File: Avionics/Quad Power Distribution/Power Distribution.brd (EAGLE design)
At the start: 50 x 50 mm, 56 parts, among them U1 LMP8645, U10 SERVOPLUGTHROUGHHOLE_0.1PITCH, U2 LMP8645, U3 LMP8645, U4 LMP8645, U5 LMP8645, U6 ADP2302, U7 SERVOPLUGTHROUGHHOLE_0.1PITCH, U8 SERVOPLUGTHROUGHHOLE_0.1PITCH, U9 SERVOPLUGTHROUGHHOLE_0.1PITCH

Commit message: Refactored power distrib board libraries into single library
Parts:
- BATT+, GND: device Shared Libraries:10AWG_SOLDERPAD -> PowerDistributionv1:10AWG_SOLDERPAD
- C1, C2, C3, C4: device SparkFun-Capacitors:0603-CAP -> PowerDistributionv1:0603-CAP
- D1: device diode:SMB -> PowerDistributionv1:SMB
- JP1: device Shared Libraries:DF13_6POS -> PowerDistributionv1:DF13_6POS
- JP2: device Shared Libraries:DF13_5POS -> PowerDistributionv1:DF13_5POS
- L1: device SparkFun-Passives:0603 -> PowerDistributionv1:0603
- R1, R2, R3, R4, R5, R6, R7, R8: device Shared Libraries:R2512 -> PowerDistributionv1:R2512
- R10, R11, R12, R13, R14, R15, R16, R17, R18, R19, R20, R21, R22, R23, R9: device Shared Libraries:0603-RES -> PowerDistributionv1:0603-RES
- U1, U2, U3, U4, U5: device Shared Libraries:SOT23-6 -> PowerDistributionv1:SOT23-6
- U10, U7, U8, U9: device Shared Libraries:0.1-PITCH-3CONN -> PowerDistributionv1:0.1-PITCH-3CONN
- U6: device Shared Libraries:SOIC8 -> PowerDistributionv1:SOIC8
- V1+, V1-, V2+, V2-, V3+, V3-, V4+, V4-: device Shared Libraries:5MMPLUG -> PowerDistributionv1:5MMPLUG

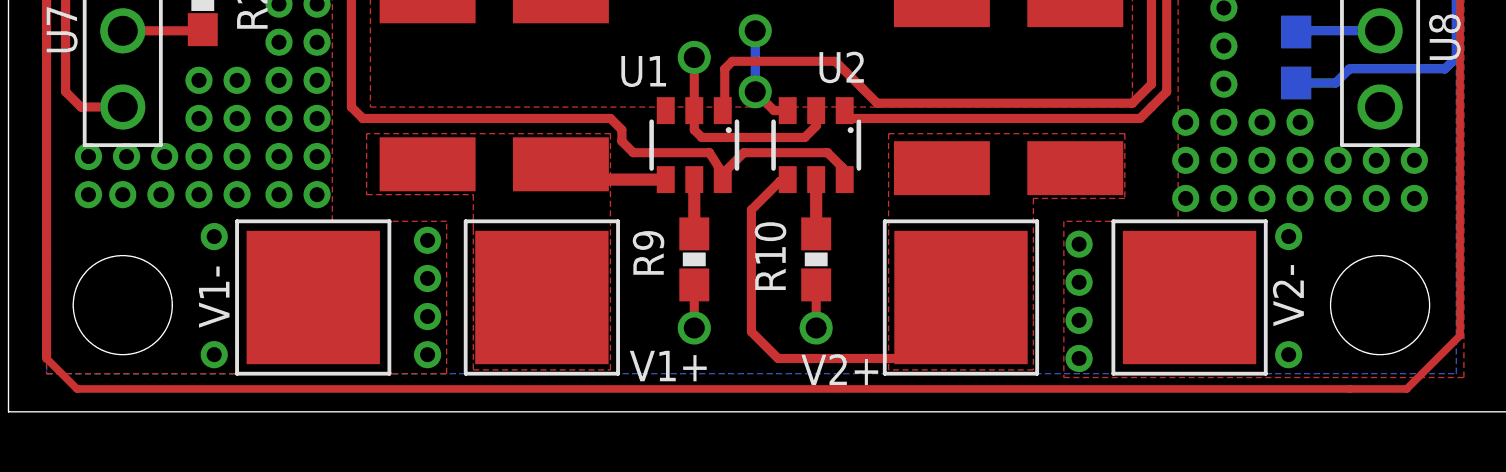
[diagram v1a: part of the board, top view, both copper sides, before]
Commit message: Updated board for model compatibility (no actual layout or part changes).
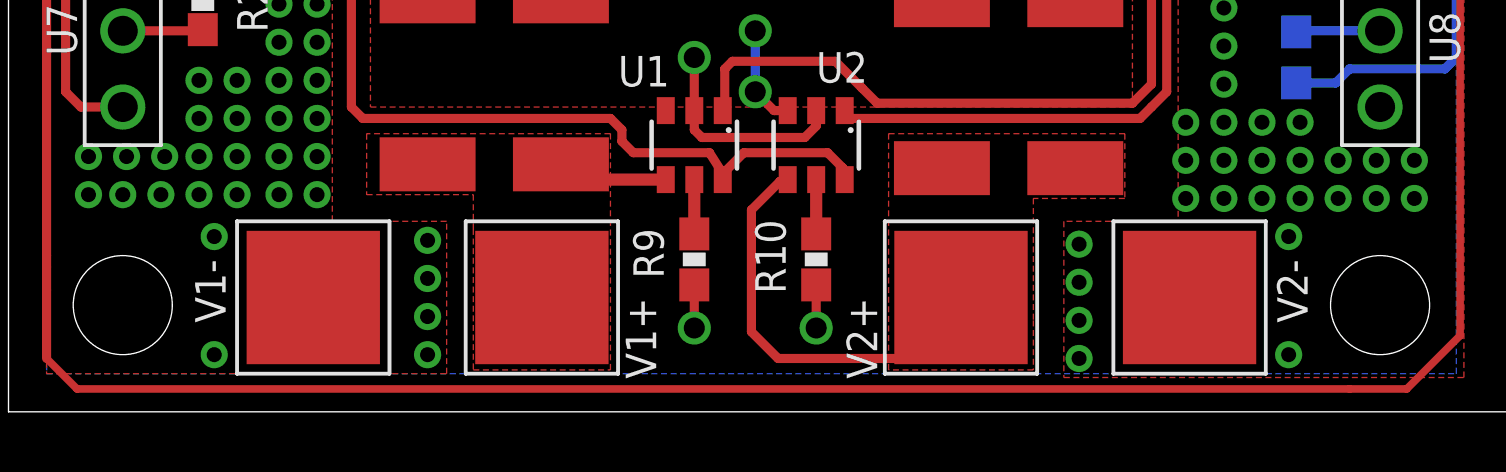
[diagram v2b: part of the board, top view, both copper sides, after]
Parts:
- U10, U7, U8, U9: device PowerDistributionv1:0.1-PITCH-3CONN -> PowerDistributionv1:0.1-PITCH-3CONN_RANGLE
- turned V1+ to 180 degrees
- turned V1- to 180 degrees
- turned V2+ to 180 degrees
- turned V2- to 180 degrees
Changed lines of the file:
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@@
 <attribute name="VALUE" x="21.59" y="36.068" size="1.27" layer="27" rot="R90" display="off"/>
 </element>
-<element name="V1+" library="PowerDistributionv1" package="5MMPLUG" value="3.5MM-BULLET-PLUG5MM-PAD" x="17.78" y="3.81" smashed="yes">
-<attribute name="NAME" x="20.701" y="1.016" size="1.016" layer="21"/>
+<element name="V1+" library="PowerDistributionv1" package="5MMPLUG" value="3.5MM-BULLET-PLUG5MM-PAD" x="17.78" y="3.81" smashed="yes" rot="R180">
+<attribute name="NAME" x="20.574" y="3.81" size="1.016" layer="21" rot="R270"/>
 </element>
-<element name="V2+" library="PowerDistributionv1" package="5MMPLUG" value="3.5MM-BULLET-PLUG5MM-PAD" x="31.75" y="3.81" smashed="yes">
-<attribute name="NAME" x="26.416" y="0.889" size="1.016" layer="21"/>
+<element name="V2+" library="PowerDistributionv1" package="5MMPLUG" value="3.5MM-BULLET-PLUG5MM-PAD" x="31.75" y="3.81" smashed="yes" rot="R180">
+<attribute name="NAME" x="27.94" y="3.81" size="1.016" layer="21" rot="R270"/>
 </element>
 <element name="V3+" library="PowerDistributionv1" package="5MMPLUG" value="3.5MM-BULLET-PLUG5MM-PAD" x="31.75" y="45.72" smashed="yes">
@@
 <attribute name="NAME" x="20.574" y="47.498" size="1.016" layer="21"/>
 </element>
-<element name="V1-" library="PowerDistributionv1" package="5MMPLUG" value="3.5MM-BULLET-PLUG5MM-PAD" x="10.16" y="3.81" smashed="yes">
-<attribute name="NAME" x="7.366" y="2.794" size="1.016" layer="21" rot="R90"/>
+<element name="V1-" library="PowerDistributionv1" package="5MMPLUG" value="3.5MM-BULLET-PLUG5MM-PAD" x="10.16" y="3.81" smashed="yes" rot="R180">
+<attribute name="NAME" x="6.223" y="5.08" size="1.016" layer="21" rot="R270"/>
 </element>
-<element name="V2-" library="PowerDistributionv1" package="5MMPLUG" value="3.5MM-BULLET-PLUG5MM-PAD" x="39.37" y="3.81" smashed="yes">
-<attribute name="NAME" x="42.164" y="4.953" size="1.016" layer="21" rot="R270"/>
+<element name="V2-" library="PowerDistributionv1" package="5MMPLUG" value="3.5MM-BULLET-PLUG5MM-PAD" x="39.37" y="3.81" smashed="yes" rot="R180">
+<attribute name="NAME" x="42.291" y="5.08" size="1.016" layer="21" rot="R270"/>
 </element>
 <element name="V3-" library="PowerDistributionv1" package="5MMPLUG" value="3.5MM-BULLET-PLUG5MM-PAD" x="39.37" y="45.72" smashed="yes">
@@
 <attribute name="VALUE" x="9.398" y="22.479" size="1.27" layer="28" rot="MR180" display="off"/>
 </element>
-<element name="U7" library="PowerDistributionv1" package="0.1-PITCH-3CONN" value="SERVOPLUGTHROUGHHOLE_0.1PITCH" x="3.81" y="12.7" smashed="yes" rot="R270">
+<element name="U7" library="PowerDistributionv1" package="0.1-PITCH-3CONN_RANGLE" value="SERVOPLUGTHROUGHHOLE_0.1PITCH" x="3.81" y="12.7" smashed="yes" rot="R270">
 <attribute name="NAME" x="1.27" y="13.589" size="1.016" layer="21" rot="R270"/>
 </element>
-<element name="U8" library="PowerDistributionv1" package="0.1-PITCH-3CONN" value="SERVOPLUGTHROUGHHOLE_0.1PITCH" x="45.72" y="12.7" smashed="yes" rot="R90">
+<element name="U8" library="PowerDistributionv1" package="0.1-PITCH-3CONN_RANGLE" value="SERVOPLUGTHROUGHHOLE_0.1PITCH" x="45.72" y="12.7" smashed="yes" rot="R90">
 <attribute name="NAME" x="47.371" y="13.335" size="1.016" layer="21" rot="R270"/>
 </element>
-<element name="U9" library="PowerDistributionv1" package="0.1-PITCH-3CONN" value="SERVOPLUGTHROUGHHOLE_0.1PITCH" x="45.72" y="36.449" smashed="yes" rot="R90">
+<element name="U9" library="PowerDistributionv1" package="0.1-PITCH-3CONN_RANGLE" value="SERVOPLUGTHROUGHHOLE_0.1PITCH" x="45.72" y="36.449" smashed="yes" rot="R90">
 <attribute name="NAME" x="45.466" y="40.64" size="1.016" layer="21"/>
 </element>
-<element name="U10" library="PowerDistributionv1" package="0.1-PITCH-3CONN" value="SERVOPLUGTHROUGHHOLE_0.1PITCH" x="3.81" y="36.449" smashed="yes" rot="R270">
+<element name="U10" library="PowerDistributionv1" package="0.1-PITCH-3CONN_RANGLE" value="SERVOPLUGTHROUGHHOLE_0.1PITCH" x="3.81" y="36.449" smashed="yes" rot="R270">
 <attribute name="NAME" x="2.413" y="40.513" size="1.016" layer="21"/>
 </element>

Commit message: Updated part references.
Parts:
- JP1: device PowerDistributionv1:DF13_6POS -> PowerDistributionv1:DF13A-6P-1.25H
- JP2: device PowerDistributionv1:DF13_5POS -> PowerDistributionv1:DF13A-5P-1.25H
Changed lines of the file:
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@@
 <layer number="220" name="220bmp" color="21" fill="1" visible="no" active="no"/>
 <layer number="221" name="221bmp" color="22" fill="1" visible="no" active="no"/>
+<layer number="222" name="222bmp" color="7" fill="1" visible="yes" active="yes"/>
 <layer number="223" name="223bmp" color="24" fill="1" visible="no" active="no"/>
 <layer number="224" name="224bmp" color="25" fill="1" visible="no" active="no"/>
@@
 <attribute name="VALUE" x="7.747" y="34.544" size="0.4064" layer="27" font="vector" rot="R90" display="off"/>
 </element>
-<element name="JP1" library="PowerDistributionv1" package="DF13_6POS" value="" x="7.112" y="24.511" smashed="yes" rot="R90">
+<element name="JP1" library="PowerDistributionv1" package="DF13A-6P-1.25H" value="" x="7.112" y="24.511" smashed="yes" rot="R90">
 <attribute name="NAME" x="5.643" y="29.853" size="1.016" layer="21"/>
 </element>
-<element name="JP2" library="PowerDistributionv1" package="DF13_5POS" value="" x="42.545" y="24.511" smashed="yes" rot="R270">
+<element name="JP2" library="PowerDistributionv1" package="DF13A-5P-1.25H" value="" x="42.545" y="24.511" smashed="yes" rot="R270">
 <attribute name="NAME" x="41.193" y="29.472" size="1.016" layer="21"/>
 </element>
